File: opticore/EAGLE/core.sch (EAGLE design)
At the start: 72 parts, among them IC1 LM2596T, J1 POWER_JACKSLT, J2 POWER_JACKSLT, Q1 2N3904, Q2 2N3904, Q3 2N3904, Q4 2N3904, Q5 2N3904, Q6 2N3904, Q7 2N3904, X1 FFKV8

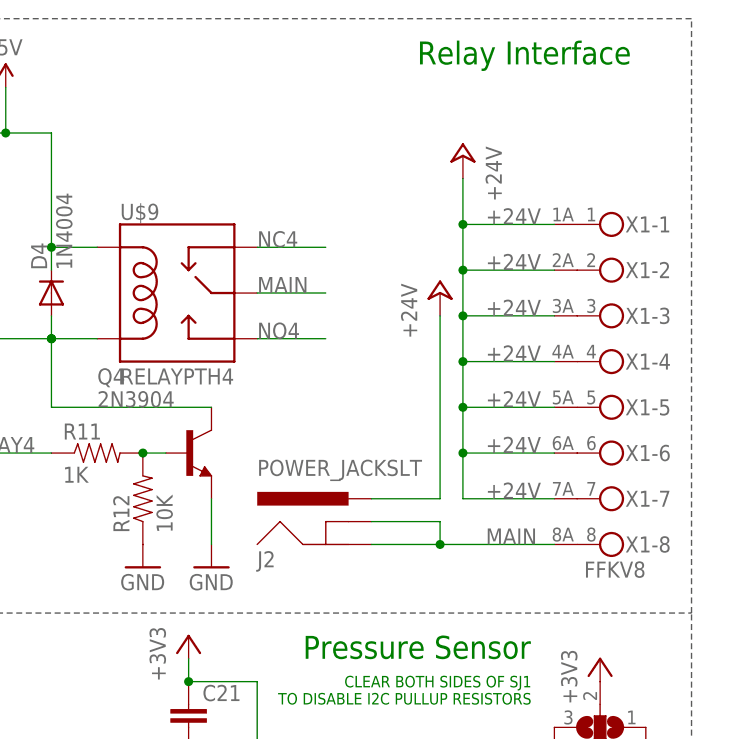
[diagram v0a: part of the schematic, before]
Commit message: Placed and Routed new 24VAC to 5VDC
Hopefully this works as expected. Horray for Rev 1!

Signed-off-by: Scott Lerner <scottphiliplerner@gmail.com>
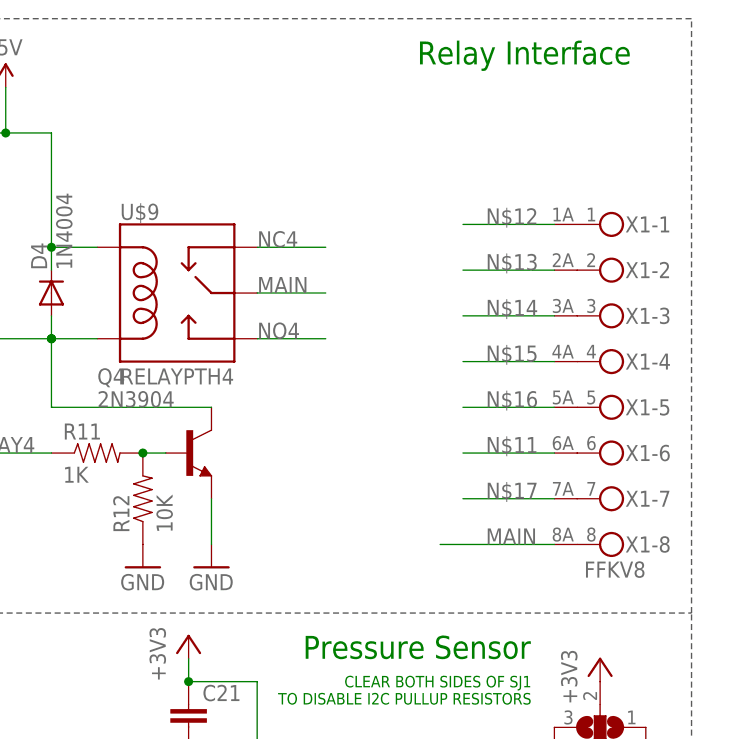
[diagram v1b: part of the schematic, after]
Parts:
- removed J2: POWER_JACKSLT, SparkFun-Connectors:POWER_JACKSLT
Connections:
- removed net +24V: J2.PWR, X1-1.2, X1-2.2, X1-3.2, X1-4.2, X1-5.2, X1-6.2, X1-7.2
- new net N$11: X1-6.2
- new net N$12: X1-1.2
- new net N$13: X1-2.2
- new net N$14: X1-3.2
- new net N$15: X1-4.2
- new net N$16: X1-5.2
- new net N$17: X1-7.2
- net MAIN: no longer J2.GND, J2.GNDBREAK
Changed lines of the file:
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@@
 <part name="LED8" library="SparkFun-LED" deviceset="LED" device="3MM"/>
 <part name="SUPPLY9" library="SparkFun-Aesthetics" deviceset="5V" device=""/>
-<part name="J2" library="SparkFun-Connectors" deviceset="POWER_JACK" device="SLT"/>
-<part name="P+1" library="supply1" deviceset="+24V" device=""/>
-<part name="P+2" library="supply1" deviceset="+24V" device=""/>
 <part name="IC1" library="national-semiconductor" deviceset="LM2596" device="T"/>
 <part name="U$1" library="adafruit" deviceset="L" device="" value="150uH"/>
@@
 <instance part="LED8" gate="G$1" x="134.62" y="20.32"/>
 <instance part="SUPPLY9" gate="G$1" x="205.74" y="71.12"/>
-<instance part="J2" gate="G$1" x="208.28" y="121.92"/>
-<instance part="P+1" gate="1" x="218.44" y="152.4"/>
-<instance part="P+2" gate="1" x="220.98" y="167.64" rot="MR0"/>
 <instance part="IC1" gate="G$1" x="58.42" y="22.86"/>
 <instance part="U$1" gate="G$1" x="86.36" y="25.4" rot="R90"/>
@@
 <label x="223.52" y="124.46" size="1.778" layer="95"/>
 <wire x1="231.14" y1="124.46" x2="218.44" y2="124.46" width="0.1524" layer="91"/>
-<pinref part="J2" gate="G$1" pin="GNDBREAK"/>
-<wire x1="218.44" y1="124.46" x2="218.44" y2="127" width="0.1524" layer="91"/>
-<wire x1="218.44" y1="127" x2="210.82" y2="127" width="0.1524" layer="91"/>
-<pinref part="J2" gate="G$1" pin="GND"/>
-<wire x1="210.82" y1="124.46" x2="218.44" y2="124.46" width="0.1524" layer="91"/>
-<junction x="218.44" y="124.46"/>
 </segment>
 </net>
@@
 </segment>
 </net>
-<net name="+24V" class="0">
-<segment>
-<pinref part="J2" gate="G$1" pin="PWR"/>
-<pinref part="P+1" gate="1" pin="+24V"/>
-<wire x1="210.82" y1="129.54" x2="218.44" y2="129.54" width="0.1524" layer="91"/>
-<wire x1="218.44" y1="129.54" x2="218.44" y2="149.86" width="0.1524" layer="91"/>
-</segment>
-<segment>
-<pinref part="X1" gate="-1" pin="2"/>
-<wire x1="231.14" y1="160.02" x2="220.98" y2="160.02" width="0.1524" layer="91"/>
-<label x="223.52" y="160.02" size="1.778" layer="95"/>
-<pinref part="P+2" gate="1" pin="+24V"/>
-<wire x1="220.98" y1="165.1" x2="220.98" y2="160.02" width="0.1524" layer="91"/>
-<pinref part="X1" gate="-2" pin="2"/>
-<wire x1="231.14" y1="154.94" x2="220.98" y2="154.94" width="0.1524" layer="91"/>
-<label x="223.52" y="154.94" size="1.778" layer="95"/>
-<wire x1="220.98" y1="160.02" x2="220.98" y2="154.94" width="0.1524" layer="91"/>
-<junction x="220.98" y="160.02"/>
-<pinref part="X1" gate="-3" pin="2"/>
-<wire x1="231.14" y1="149.86" x2="220.98" y2="149.86" width="0.1524" layer="91"/>
-<label x="223.52" y="149.86" size="1.778" layer="95"/>
-<wire x1="220.98" y1="154.94" x2="220.98" y2="149.86" width="0.1524" layer="91"/>
-<junction x="220.98" y="154.94"/>
-<pinref part="X1" gate="-4" pin="2"/>
-<wire x1="231.14" y1="144.78" x2="220.98" y2="144.78" width="0.1524" layer="91"/>
-<label x="223.52" y="144.78" size="1.778" layer="95"/>
-<wire x1="220.98" y1="149.86" x2="220.98" y2="144.78" width="0.1524" layer="91"/>
-<junction x="220.98" y="149.86"/>
-<pinref part="X1" gate="-5" pin="2"/>
-<wire x1="231.14" y1="139.7" x2="220.98" y2="139.7" width="0.1524" layer="91"/>
-<label x="223.52" y="139.7" size="1.778" layer="95"/>
-<wire x1="220.98" y1="144.78" x2="220.98" y2="139.7" width="0.1524" layer="91"/>
-<junction x="220.98" y="144.78"/>
-<pinref part="X1" gate="-6" pin="2"/>
-<wire x1="231.14" y1="134.62" x2="220.98" y2="134.62" width="0.1524" layer="91"/>
-<label x="223.52" y="134.62" size="1.778" layer="95"/>
-<wire x1="220.98" y1="139.7" x2="220.98" y2="134.62" width="0.1524" layer="91"/>
-<junction x="220.98" y="139.7"/>
-<pinref part="X1" gate="-7" pin="2"/>
-<wire x1="231.14" y1="129.54" x2="220.98" y2="129.54" width="0.1524" layer="91"/>
-<label x="223.52" y="129.54" size="1.778" layer="95"/>
-<wire x1="220.98" y1="134.62" x2="220.98" y2="129.54" width="0.1524" layer="91"/>
-<junction x="220.98" y="134.62"/>
-</segment>
-</net>
 <net name="NO4" class="0">
 <segment>
@@
 </segment>
 </net>
+<net name="N$11" class="0">
+<segment>
+<pinref part="X1" gate="-6" pin="2"/>
+<wire x1="231.14" y1="134.62" x2="220.98" y2="134.62" width="0.1524" layer="91"/>
+<label x="223.52" y="134.62" size="1.778" layer="95"/>
+</segment>
+</net>
+<net name="N$12" class="0">
+<segment>
+<pinref part="X1" gate="-1" pin="2"/>
+<wire x1="231.14" y1="160.02" x2="220.98" y2="160.02" width="0.1524" layer="91"/>
+<label x="223.52" y="160.02" size="1.778" layer="95"/>
+</segment>
+</net>
+<net name="N$13" class="0">
+<segment>
+<pinref part="X1" gate="-2" pin="2"/>
+<wire x1="231.14" y1="154.94" x2="220.98" y2="154.94" width="0.1524" layer="91"/>
+<label x="223.52" y="154.94" size="1.778" layer="95"/>
+</segment>
+</net>
+<net name="N$14" class="0">
+<segment>
+<pinref part="X1" gate="-3" pin="2"/>
+<wire x1="231.14" y1="149.86" x2="220.98" y2="149.86" width="0.1524" layer="91"/>
+<label x="223.52" y="149.86" size="1.778" layer="95"/>
+</segment>
+</net>
+<net name="N$15" class="0">
+<segment>
+<pinref part="X1" gate="-4" pin="2"/>
+<wire x1="231.14" y1="144.78" x2="220.98" y2="144.78" width="0.1524" layer="91"/>
+<label x="223.52" y="144.78" size="1.778" layer="95"/>
+</segment>
+</net>
+<net name="N$16" class="0">
+<segment>
+<pinref part="X1" gate="-5" pin="2"/>
+<wire x1="231.14" y1="139.7" x2="220.98" y2="139.7" width="0.1524" layer="91"/>
+<label x="223.52" y="139.7" size="1.778" layer="95"/>
+</segment>
+</net>
+<net name="N$17" class="0">
+<segment>
+<pinref part="X1" gate="-7" pin="2"/>
+<wire x1="231.14" y1="129.54" x2="220.98" y2="129.54" width="0.1524" layer="91"/>
+<label x="223.52" y="129.54" size="1.778" layer="95"/>
+</segment>
+</net>

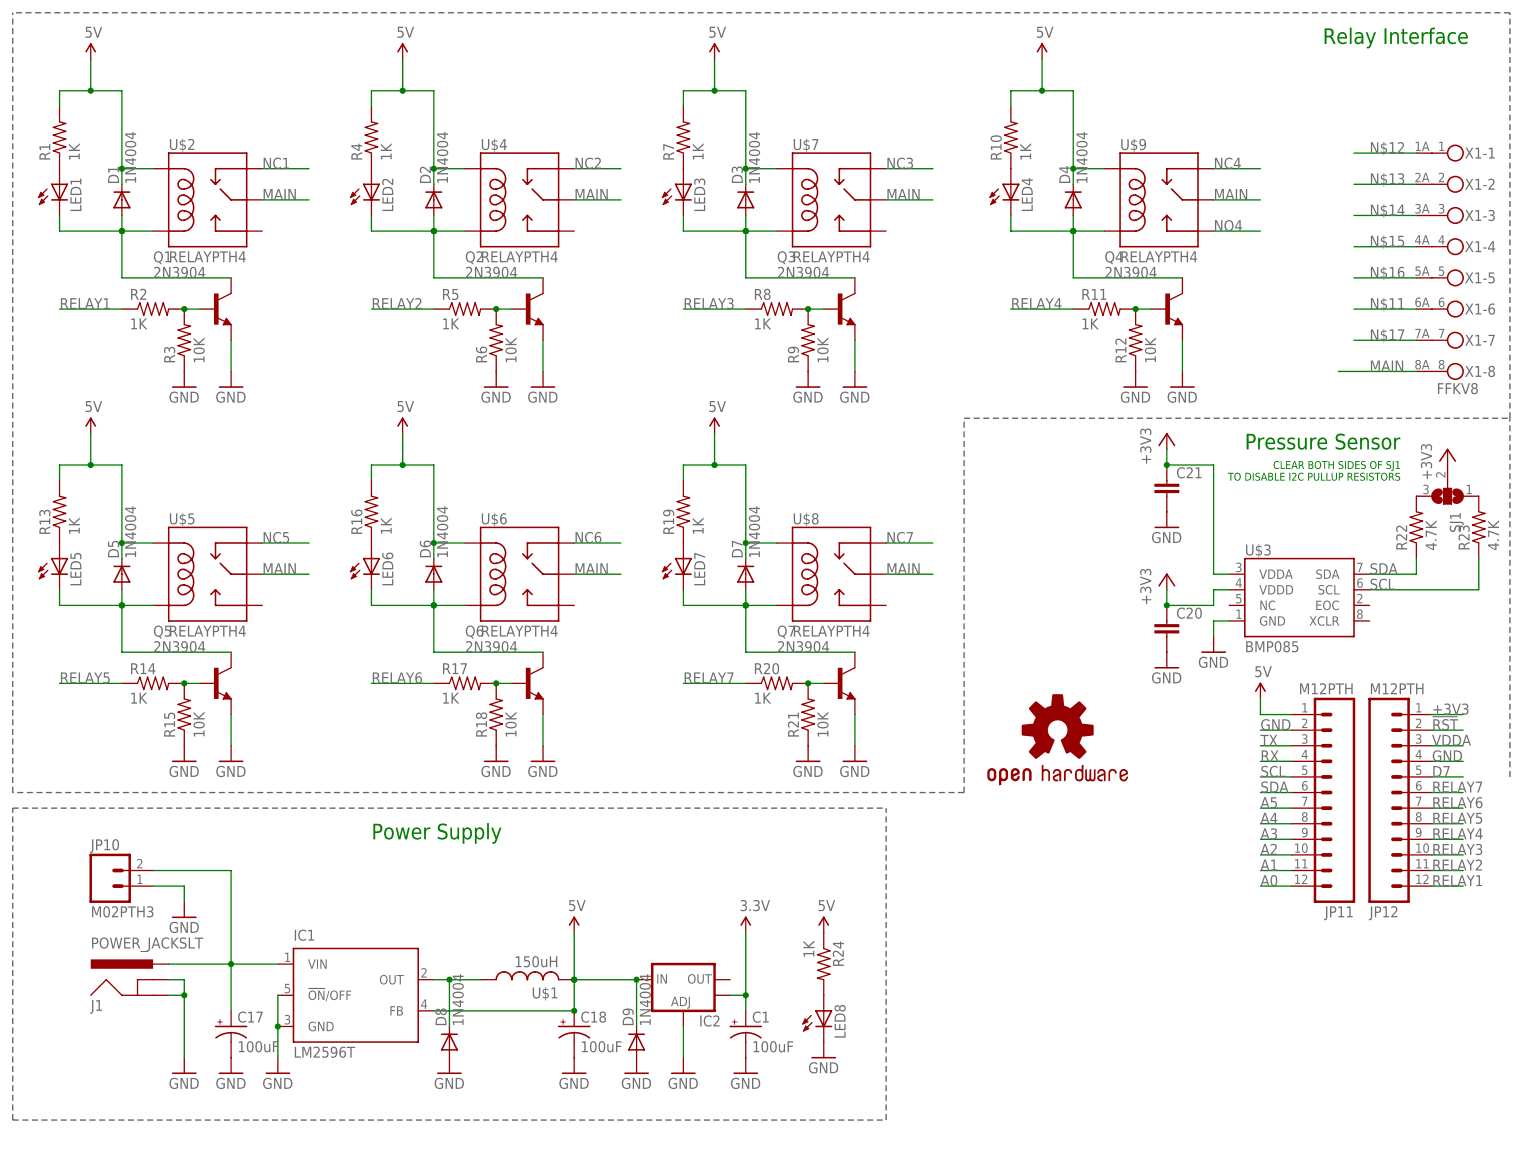
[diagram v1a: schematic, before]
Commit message: Added TRIACS instead of Relays
In theory this will work more efficiently. Hopefully it does.
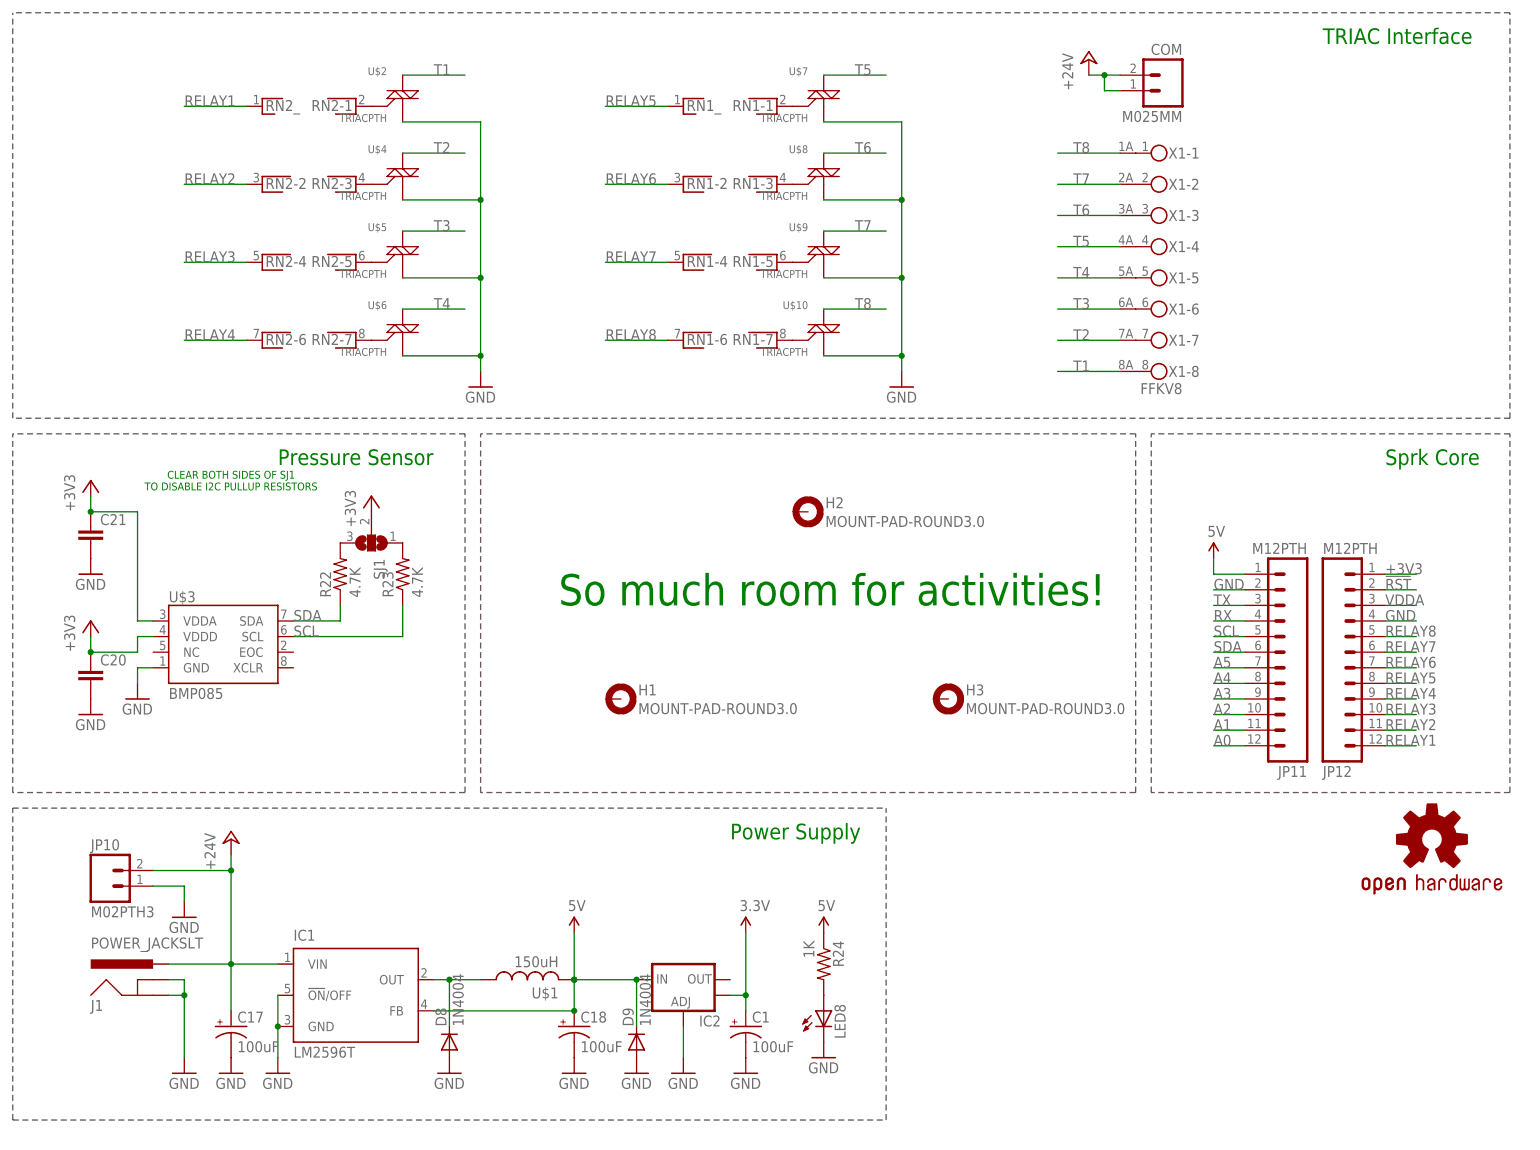
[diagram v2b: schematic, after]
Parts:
- removed D1, D2, D3, D4, D5, D6, D7: 1N4004, diode:1N4004
- removed LED1, LED2, LED3, LED4, LED5, LED6, LED7: (no value), SparkFun-LED:LED3MM
- removed Q1, Q2, Q3, Q4, Q5, Q6, Q7: 2N3904, transistor-npn:2N3904
- removed R1, R10, R11, R13, R14, R16, R17, R19, R2, R20, R4, R5, R7, R8: 1K, SparkFun-Resistors:RESISTORAXIAL-0.3
- removed R12, R15, R18, R21, R3, R6, R9: 10K, SparkFun-Resistors:RESISTORAXIAL-0.3
- added COM: M025MM, SparkFun-Connectors:M025MM
- added H1, H2, H3: MOUNT-PAD-ROUND3.0, holes:MOUNT-PAD-ROUND3.0
- added RN1, RN2: (no value), resistor-net:RNX7
- added U$10: TRIACPTH, SparkFun-DiscreteSemi:TRIACPTH
- U$2, U$4, U$5, U$6, U$7, U$8, U$9: value RELAYPTH4 -> TRIACPTH; device SparkFun-Electromechanical:RELAYPTH4 -> SparkFun-DiscreteSemi:TRIACPTH
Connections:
- removed net D7: JP12.5
- removed net MAIN: U$2.MAIN, U$4.MAIN, U$5.MAIN, U$6.MAIN, U$7.MAIN, U$8.MAIN, U$9.MAIN, X1-8.2
- removed net N$11: X1-6.2
- removed net N$12: X1-1.2
- removed net N$13: X1-2.2
- removed net N$14: X1-3.2
- removed net N$15: X1-4.2
- removed net N$16: X1-5.2
- removed net N$17: X1-7.2
- removed net N$19: D2.A, LED2.C, Q2.C, U$4.COIL2
- removed net N$20: Q2.B, R5.2, R6.2
- removed net N$22: D5.A, LED5.C, Q5.C, U$5.COIL2
- removed net N$23: Q5.B, R14.2, R15.2
- removed net N$24: Q1.B, R2.2, R3.2
- removed net N$26: D6.A, LED6.C, Q6.C, U$6.COIL2
- removed net N$27: Q6.B, R17.2, R18.2
- removed net N$29: D3.A, LED3.C, Q3.C, U$7.COIL2
- removed net N$30: Q3.B, R8.2, R9.2
- removed net N$32: D7.A, LED7.C, Q7.C, U$8.COIL2
- removed net N$33: Q7.B, R20.2, R21.2
- removed net N$35: D4.A, LED4.C, Q4.C, U$9.COIL2
- removed net N$36: Q4.B, R11.2, R12.2
- removed net N$37: C17.+, IC1.VIN, J1.PWR, JP10.2
- removed net NC1: U$2.NC
- removed net NC2: U$4.NC
- removed net NC3: U$7.NC
- removed net NC4: U$9.NC
- removed net NC5: U$5.NC
- removed net NC6: U$6.NC
- removed net NC7: U$8.NC
- removed net NO4: U$9.NO
- new net +24V: C17.+, COM.1, COM.2, IC1.VIN, J1.PWR, JP10.2
- new net RELAY8: JP12.5, RN1-6.1
- new net T1: U$2.M2, X1-8.2
- new net T2: U$4.M2, X1-7.2
- new net T3: U$5.M2, X1-6.2
- new net T4: U$6.M2, X1-5.2
- new net T5: U$7.M2, X1-4.2
- new net T6: U$8.M2, X1-3.2
- new net T7: U$9.M2, X1-2.2
- new net T8: U$10.M2, X1-1.2
- net 5V: no longer D1.C, D2.C, D3.C, D4.C, D5.C, D6.C, D7.C, R1.2, R10.2, R13.2, R16.2, R19.2, R4.2, R7.2, U$2.COIL1, U$4.COIL1, U$5.COIL1, U$6.COIL1, U$7.COIL1, U$8.COIL1, U$9.COIL1
- net GND: now also U$10.M1, U$2.M1, U$4.M1, U$5.M1, U$6.M1, U$7.M1, U$8.M1, U$9.M1; no longer Q1.E, Q2.E, Q3.E, Q4.E, Q5.E, Q6.E, Q7.E, R12.1, R15.1, R18.1, R21.1, R3.1, R6.1, R9.1
- net N$1: now also RN1-3.1, U$8.G; no longer LED1.A, R1.1
- net N$18: now also RN1-7.1, U$10.G; no longer D1.A, LED1.C, Q1.C, U$2.COIL2
- net N$2: now also RN1-1.1, U$7.G; no longer LED2.A, R4.1
- net N$3: now also RN2-1.1, U$2.G; no longer LED5.A, R13.1
- net N$4: now also RN2-3.1, U$4.G; no longer LED6.A, R16.1
- net N$5: now also RN2-5.1, U$5.G; no longer LED3.A, R7.1
- net N$6: now also RN2-7.1, U$6.G; no longer LED4.A, R10.1
- net N$7: now also RN1-5.1, U$9.G; no longer LED7.A, R19.1
- net RELAY1: now also RN2_.1; no longer R2.1
- net RELAY2: now also RN2-2.1; no longer R5.1
- net RELAY3: now also RN2-4.1; no longer R8.1
- net RELAY4: now also RN2-6.1; no longer R11.1
- net RELAY5: now also RN1_.1; no longer R14.1
- net RELAY6: now also RN1-2.1; no longer R17.1
- net RELAY7: now also RN1-4.1; no longer R20.1
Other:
- note added: "So much room for activities!"
- note added: "Sprk Core"
- note added: "TRIAC Interface"
- note removed: "Relay Interface"
- moved on the sheet: C20, C21, JP11, JP12, R22, R23, SJ1, U$3, X1-1, X1-2, X1-3, X1-4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

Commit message: Trying to get to a finished v1.0
Added silkscreen and tried to generate Gerber files. Committing for other computer.

Signed-off-by: Scott Lerner <scottphiliplerner@gmail.com>
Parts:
- removed C17: 100uF, SparkFun-Passives:CAP_POLPTH1
- added C3: 100uF, SparkFun-Passives:CAP_POLPTH1
- renumbered C18 to C2, C20 to C5, C21 to C4, D8 to D1, D9 to D2, LED8 to D3, R22 to R2, R23 to R3, R24 to R1, U$1 to L1, U$10 to T8, U$2 to T1, U$4 to T2, U$5 to T3, U$6 to T4, U$7 to T5, U$8 to T6, U$9 to T7
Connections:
- net +24V: now also C1.+; no longer C17.+
- net 3.3V: now also C3.+; no longer C1.+
- net GND: now also C3.-; no longer C17.-
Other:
- moved on the sheet: C1

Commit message: Sending my baby off to the board house!
Version 1.0 of the board is done and is being prepped for the board house. Just trying to decide on who to print with...

Signed-off-by: Scott Lerner <scottphiliplerner@gmail.com>
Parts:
- removed H3: MOUNT-PAD-ROUND3.0, holes:MOUNT-PAD-ROUND3.0
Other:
- note added: "1.0"
- note added: "1/1"
- note added: "11/1/13"
- note added: "Gardener TRIAC v1.0"
- note added: "Opti-Lawn Gardener"
- moved on the sheet: H2
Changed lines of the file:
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@@
 <part name="H1" library="holes" deviceset="MOUNT-PAD-ROUND" device="3.0"/>
 <part name="H2" library="holes" deviceset="MOUNT-PAD-ROUND" device="3.0"/>
-<part name="H3" library="holes" deviceset="MOUNT-PAD-ROUND" device="3.0"/>
+<part name="+3V1" library="supply1" deviceset="+3V3" device=""/>
 </parts>
 <sheets>
@@
 <wire x1="78.74" y1="55.88" x2="78.74" y2="114.3" width="0.1524" layer="97" style="dashdot"/>
 <wire x1="185.42" y1="55.88" x2="185.42" y2="114.3" width="0.1524" layer="97" style="dashdot"/>
+<text x="152.4" y="25.4" size="5.08" layer="91" font="vector">Opti-Lawn Gardener</text>
+<text x="238.76" y="7.62" size="2.54" layer="91">1.0</text>
+<text x="165.1" y="17.78" size="2.54" layer="91">Gardener TRIAC v1.0</text>
+<text x="160.02" y="1.27" size="2.54" layer="91">11/1/13</text>
+<text x="233.68" y="1.27" size="2.54" layer="91">1/1</text>
 </plain>
 <instances>
 <instance part="FRAME1" gate="G$1" x="0" y="0"/>
-<instance part="FRAME1" gate="G$2" x="147.32" y="0"/>
+<instance part="FRAME1" gate="G$2" x="147.32" y="0" smashed="yes"/>
 <instance part="U$3" gate="G$1" x="35.56" y="81.28"/>
 <instance part="J1" gate="G$1" x="25.4" y="20.32"/>
@@
 <instance part="GND6" gate="1" x="147.32" y="121.92"/>
 <instance part="H1" gate="G$1" x="101.6" y="71.12"/>
-<instance part="H2" gate="G$1" x="132.08" y="101.6"/>
-<instance part="H3" gate="G$1" x="154.94" y="71.12"/>
+<instance part="H2" gate="G$1" x="152.4" y="71.12"/>
+<instance part="+3V1" gate="G$1" x="231.14" y="96.52"/>
 </instances>
 <busses>
@@
 <segment>
 <wire x1="226.06" y1="91.44" x2="231.14" y2="91.44" width="0.1524" layer="91"/>
-<label x="226.06" y="91.44" size="1.778" layer="95"/>
 <pinref part="JP12" gate="G$1" pin="1"/>
+<pinref part="+3V1" gate="G$1" pin="+3V3"/>
+<wire x1="231.14" y1="91.44" x2="231.14" y2="93.98" width="0.1524" layer="91"/>
 </segment>
 </net>
